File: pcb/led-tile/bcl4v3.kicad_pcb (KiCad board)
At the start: 2 copper layers, 38 x 38 mm, 39 parts, among them J1 Conn_01x04, J10 Conn_01x04, J2 Conn_01x04, J3 Conn_01x04, J4 Conn_01x04, J5 10118194-0001LF, J6 Conn_01x04, J7 Conn_01x04, J8 Conn_01x05, J9 Conn_01x04, Q1 IRLML6402, U1 MCP1703A-3302_SOT23, U2 STM32F072CBUx, U3 IS31FL3730-QFSL2, Y1 ABS07-120-32.768KHZ-Z

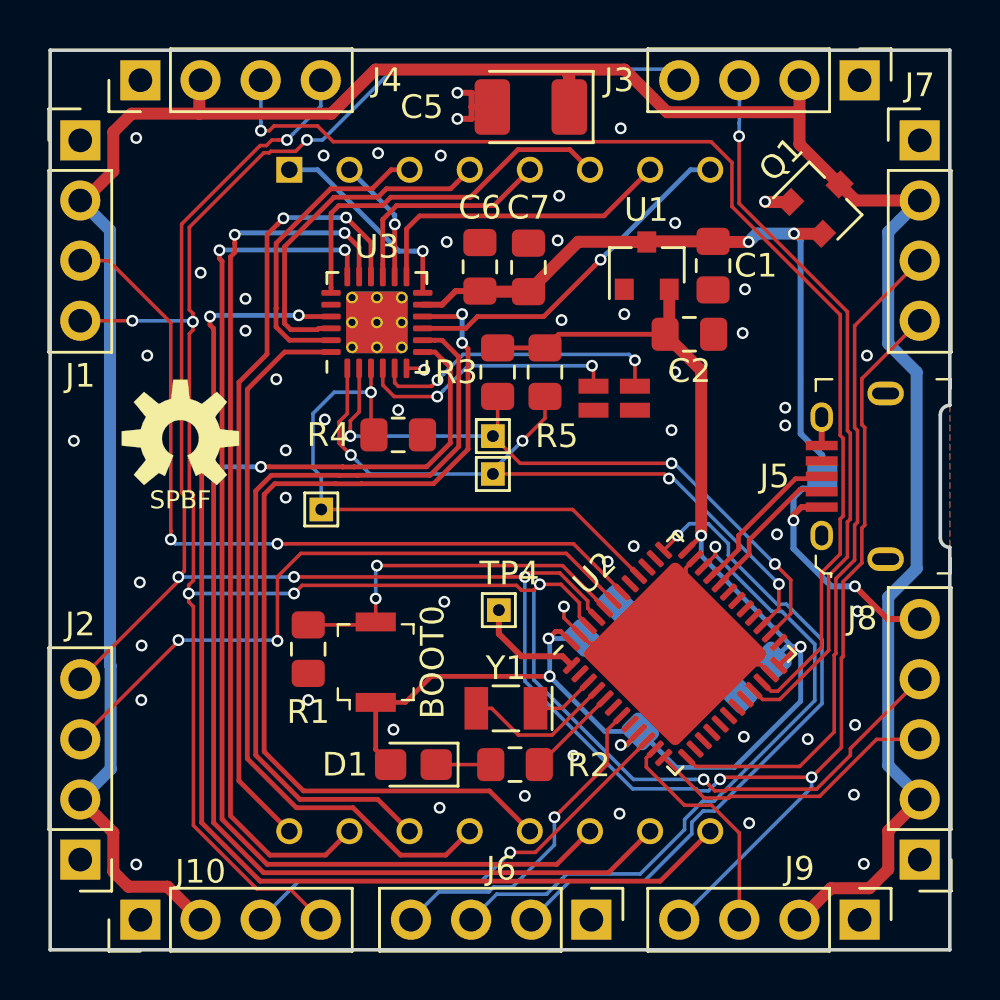
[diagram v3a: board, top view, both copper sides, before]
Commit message: Variant of the tile with integrated LED matrix driver
Use ISSI IS31FL3736 instead of discrete ICs for driving the
LED matrix
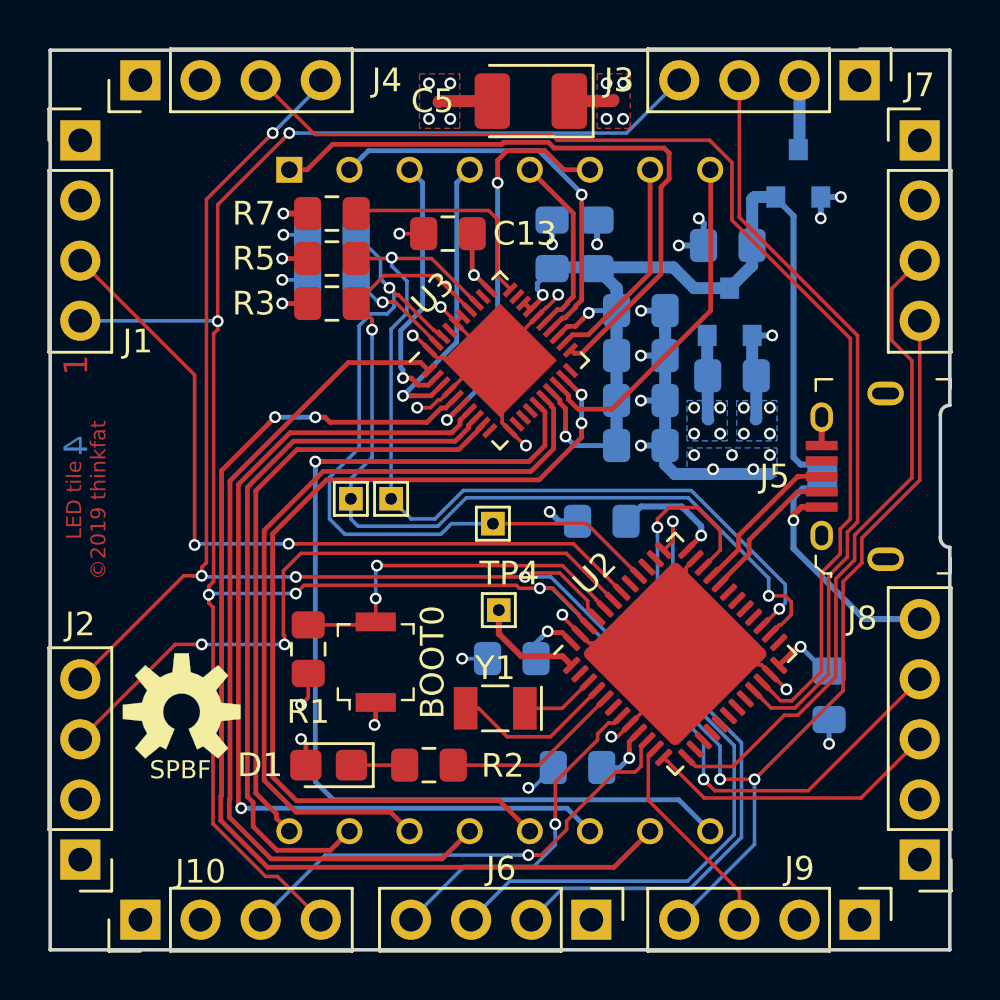
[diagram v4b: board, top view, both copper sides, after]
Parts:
- removed JP2, JP3: Jumper_2_Open, project:SMT-JUMPER_2_NC_TRACE_NO-SILK
- added C10: 100n, Capacitor_SMD:C_0805_2012Metric_Pad1.15x1.40mm_HandSolder, B.Cu at (138.9, 78.8)
- added C11: 1µF, Capacitor_SMD:C_0805_2012Metric_Pad1.15x1.40mm_HandSolder, B.Cu at (138.9, 76.9)
- added C12: 100n, Capacitor_SMD:C_0805_2012Metric_Pad1.15x1.40mm_HandSolder, B.Cu at (138.9, 75.0)
- added C13: 1µF, Capacitor_SMD:C_0805_2012Metric_Pad1.15x1.40mm_HandSolder, F.Cu at (130.8, 71.8)
- added C14: 100n, Capacitor_SMD:C_0805_2012Metric_Pad1.15x1.40mm_HandSolder, B.Cu at (137.3, 83.9)
- added C9: 1µF, Capacitor_SMD:C_0805_2012Metric_Pad1.15x1.40mm_HandSolder, B.Cu at (138.9, 80.7)
- added R6: 100k, Resistor_SMD:R_0805_2012Metric_Pad1.15x1.40mm_HandSolder, B.Cu at (125.9, 73.7)
- added R7: 22k, Resistor_SMD:R_0805_2012Metric_Pad1.15x1.40mm_HandSolder, F.Cu at (125.9, 70.9)
- C1, C2, C6, C7, Q1, R4, U1: moved to B.Cu
- R3, R5: value 4k7 -> 1k
- U3: value IS31FL3730-QFSL2 -> IS31FL3736-QFLS4; footprint project:QFN-24-1EP_4x4mm_P0.5mm_EP2.6x2.6mm_ThermalVias -> project:QFN-40_EP_5x5_Pitch0.4mm
- moved LOGO1 11.6 mm to (119.5, 92.0)
- moved R5 10.2 mm to (125.9, 72.8), turned to 0 degrees
- moved R4 8.90 mm to (125.9, 71.8), turned to 180 degrees
- moved R3 7.58 mm to (125.9, 74.7), turned to 0 degrees
- moved TP3 7.27 mm to (132.7, 84.0)
- moved TP1 6.56 mm to (126.7, 83.0)
- moved U3 5.44 mm to (133.0, 77.1), turned to 45 degrees
- moved TP2 4.43 mm to (128.4, 83.0)
- moved C3 4.06 mm to (136.3, 94.3), turned to 180 degrees
- moved C8 4.03 mm to (133.5, 89.7), turned to 180 degrees
- moved U1 4.01 mm to (142.7, 75.0)
- moved R2 3.63 mm to (130.0, 94.2)
- moved D1 3.58 mm to (125.8, 94.2)
- moved C6 3.19 mm to (135.2, 72.2)
- moved C4 3.19 mm to (146.9, 91.2), turned to 270 degrees
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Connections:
- U2 pad 8: Net-(U2-Pad8) -> GND
- U3 pad 1: /MCU_SDA -> /COL_1
- U3 pad 10: /ROW_4 -> Net-(U3-Pad10)
- U3 pad 11: +5V -> GND
- U3 pad 12: /ROW_5 -> Net-(U3-Pad12)
- U3 pad 13: /ROW_6 -> Net-(U3-Pad13)
- U3 pad 14: /ROW_7 -> Net-(U3-Pad14)
- U3 pad 15: /ROW_8 -> /ROW_1
- U3 pad 16: /COL_8 -> /ROW_2
- U3 pad 17: /COL_7 -> +5V
- U3 pad 18: /COL_6 -> /ROW_3
- U3 pad 19: /COL_5 -> /ROW_4
- U3 pad 2: /MCU_SCL -> /COL_2
- U3 pad 20: GND -> Net-(U3-Pad20)
- U3 pad 21: /COL_4 -> /ROW_5
- U3 pad 22: /COL_3 -> /ROW_6
- U3 pad 23: /COL_2 -> +5V
- U3 pad 24: /COL_1 -> /ROW_7
- U3 pad 25: GND -> /ROW_8
- U3 pad 3: /MCU_SDB -> /COL_3
- U3 pad 4: Net-(JP2-Pad2) -> GND
- U3 pad 5: Net-(JP3-Pad2) -> /COL_4
- U3 pad 6: GND -> /COL_5
- U3 pad 7: /ROW_1 -> /COL_6
- U3 pad 8: /ROW_2 -> /COL_7
- U3 pad 9: /ROW_3 -> /COL_8
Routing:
- net VCC: track 116.3 -> 4.85 mm, vias 0 -> 4
- net GND: track 21.0 -> 88.8 mm, vias 54 -> 41
- net +3V3: track 61.9 -> 24.2 mm, vias 5 -> 13
- net /ROW_5: track 8.82 -> 27.2 mm, vias 1 -> 0
- net +5V: track 28.4 -> 46.7 mm, vias 2 -> 3
- net Net-(JP3-Pad2): track 12.6 -> 0.00 mm, vias 2 -> 0
- net /ROW_7: track 5.31 -> 17.3 mm
- net Net-(JP2-Pad2): track 11.2 -> 0.00 mm, vias 2 -> 0
- net /ROW_1: track 54.0 -> 42.9 mm, vias 2 -> 1
- net /MCU_SCL: track 28.5 -> 38.9 mm, vias 3 -> 2
- net Net-(R7-Pad1): track 0.00 -> 9.37 mm
- net /MCU_SDB: track 24.0 -> 31.7 mm
- net /COL_6: track 47.5 -> 39.9 mm, vias 2 -> 1
- net /COL_8: track 33.1 -> 25.7 mm, vias 2 -> 0
- net /COL_7: track 37.5 -> 30.2 mm, vias 2 -> 0
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- added copper zone on B.Cu, net +3V3
- added copper zone on In2.Cu, net +3V3
- added copper zone on In1.Cu, net GND
- added copper zone on F.Cu, net VCC
- added copper zone on In2.Cu, net VCC
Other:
- copper layers 2 -> 4
- board text added: "1"
- board text added: "2"
- board text added: "3"
- board text added: "4"
